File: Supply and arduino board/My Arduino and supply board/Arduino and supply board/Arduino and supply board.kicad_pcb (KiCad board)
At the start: 2 copper layers, 65 parts, among them IC1 MC33269ST-5.0T3, IC2 MC33269D-5.0, J1 Barrel_Jack_MountingPin, Q1 16MHz, Q2 16MHz, T1 FDN340V, U1 LP2985-3.3, U1A1 LM358D, U1B1 LM358D, U1C1 LM358D, U3 ATmega16U2-MU, X1 USB_B, Y1 16MHz, Y2 16MHz

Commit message: new work on arduino board
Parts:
- added @HOLE0: , , F.Cu at (198.3, 64.1)
- added @HOLE1: , , F.Cu at (198.3, 92.1)
- added @HOLE2: , , F.Cu at (147.5, 48.9)
- added @HOLE3: , , F.Cu at (146.2, 97.1)
- moved ZIC1 149.8 mm to (196.1, 79.7), turned to 270 degrees
- moved IOL1 130.4 mm to (195.7, 48.9), turned to 270 degrees
- moved AD1 122.1 mm to (183.0, 97.2), turned to 90 degrees
- moved IOH1 113.4 mm to (174.1, 48.9), turned to 270 degrees
- moved ISCP2 111.7 mm to (195.8, 69.2)
- moved RN2B1 111.6 mm to (162.8, 53.3), turned to 90 degrees
- moved Q2 108.1 mm to (169.1, 57.2)
- moved POWER1 101.7 mm to (165.2, 97.2), turned to 90 degrees
- moved R3 96.9 mm to (151.6, 70.9)
- moved U1 95.7 mm to (175.5, 62.7)
- moved R1 84.6 mm to (153.7, 70.9)
- moved TX_YELLOW1 82.0 mm to (162.5, 67.1)
- moved X1 76.7 mm to (138.6, 61.6), turned to 270 degrees
- moved C5 74.8 mm to (160.6, 60.2), turned to 270 degrees
- moved PC1 74.7 mm to (150.0, 90.8), turned to 90 degrees
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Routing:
- net GND: track 0.00 -> 242.6 mm, vias 0 -> 3
- net +5V: track 0.00 -> 146.2 mm
- net /SCK: track 0.00 -> 128.6 mm, vias 0 -> 1
- net /MISO: track 0.00 -> 123.6 mm
- net /MOSI: track 0.00 -> 115.6 mm
- net /AREF: track 0.00 -> 106.2 mm
- net /RESET: track 0.00 -> 76.2 mm
- net /SS: track 0.00 -> 65.7 mm
- net /XTAL2: track 0.00 -> 61.5 mm, vias 0 -> 1
- net /IO9: track 0.00 -> 59.1 mm
- net /VIN: track 0.00 -> 51.9 mm
- net /IO8: track 0.00 -> 50.8 mm
- net /IO7: track 0.00 -> 45.9 mm
- net /IO6: track 0.00 -> 43.1 mm
- net /IO5: track 0.00 -> 40.2 mm
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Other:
- board outline added: 68.6 x 53.3 mm
- rule pad_to_mask_clearance: 0 -> 0.051
- board text added: "#"
- board text added: "0"
- board text added: "1"
- board text added: "10"
- board text added: "2"
- board text added: "2011-3-02"
- board text added: "3"
- board text added: "3V3"
- board text added: "4"
- board text added: "5"
- board text added: "5V"
- board text added: "6"
- board text added: "7"
- board text added: "8"
- board text added: "9"
- board text added: "A0"
- board text added: "A1"
- board text added: "A2"
- board text added: "A3"
- board text added: "A4"
- board text added: "A5"
- board text added: "ANALOG IN"
- board text added: "AREF"
- board text added: "D.Cuartielles"
- board text added: "D.Mellis"
- board text added: "D:/SmartProjects/Snc/a4_bn_logo2.bmp"
- board text added: "G.Martino"
- board text added: "GND"
- board text added: "IOREF"
- board text added: "ITALY"
- board text added: "M.Banzi"
- board text added: "MADE IN"
- board text added: "RESET"
- board text added: "RX"
- board text added: "SCL"
- board text added: "SDA"
- board text added: "T.Igoe"
- board text added: "TX"
- board text added: "VIN"

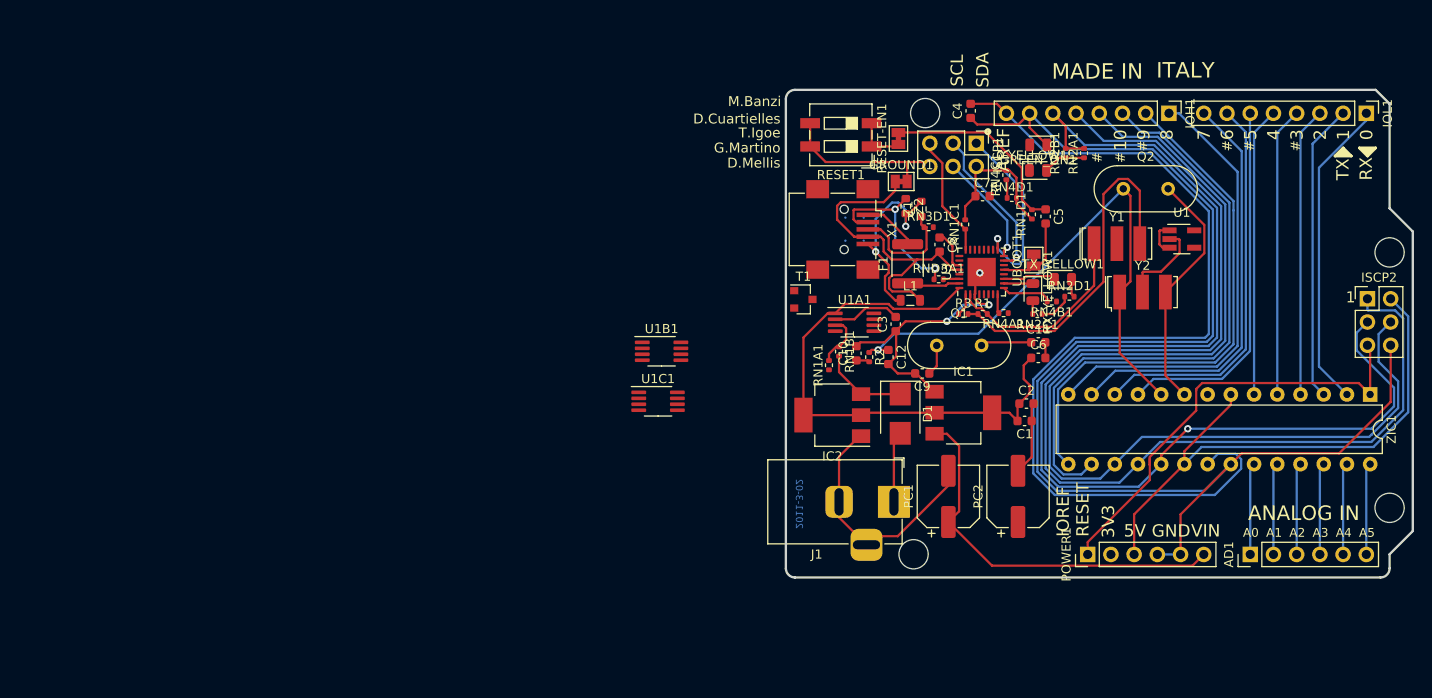
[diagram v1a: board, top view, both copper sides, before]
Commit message: every part on board is connected
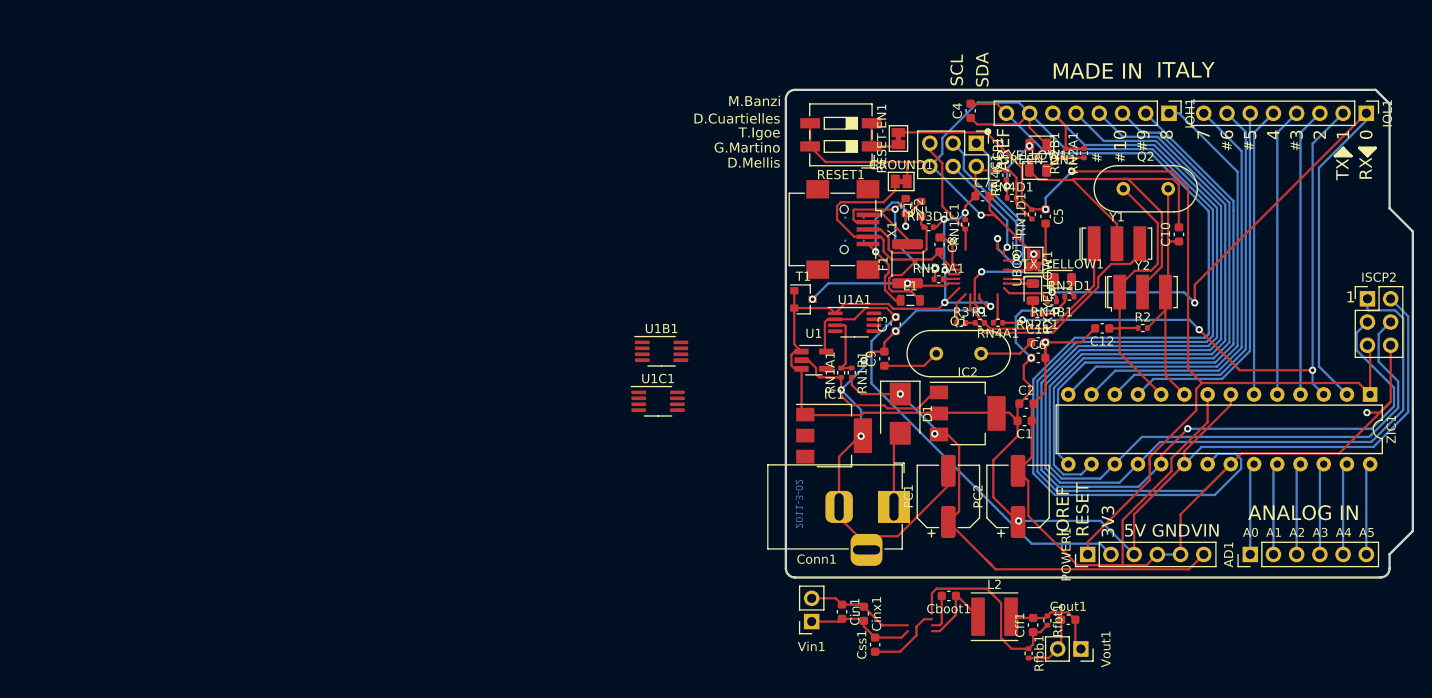
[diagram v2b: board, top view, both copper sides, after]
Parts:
- removed @HOLE0, @HOLE1, @HOLE2, @HOLE3: , 
- removed J1: Barrel_Jack_MountingPin, Connector_BarrelJack:BarrelJack_Horizontal
- removed U3: ATmega16U2-MU, Package_DFN_QFN:QFN-32-1EP_5x5mm_P0.5mm_EP3.1x3.1mm
- added Cboot1: 100n, Capacitor_SMD:C_0603_1608Metric, F.Cu at (150.0, 101.7)
- added Cff1: 47p, Capacitor_SMD:C_0603_1608Metric, F.Cu at (159.3, 104.9)
- added Cin1: 10u, Capacitor_SMD:C_0603_1608Metric, F.Cu at (138.4, 103.4)
- added Cinx1: 100n, Capacitor_SMD:C_0603_1608Metric, F.Cu at (140.7, 103.6)
- added Conn1: Connector_Barrel_Jack_MountingPin-Arduino_and_supply_board-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, Connector_BarrelJack:BarrelJack_Horizontal, F.Cu at (144.0, 92.0)
- added Cout1: 47u, Capacitor_SMD:C_0603_1608Metric, F.Cu at (163.1, 104.3)
- added Css1: 33n, Capacitor_SMD:C_0603_1608Metric, F.Cu at (142.0, 107.0)
- added L2: 15u, Inductor_SMD:L_Taiyo-Yuden_MD-5050, F.Cu at (155.0, 104.0)
- added Rfbb1: 10K, Resistor_SMD:R_0402_1005Metric, F.Cu at (158.8, 108.0)
- added Rfbt1: 140K, Resistor_SMD:R_0402_1005Metric, F.Cu at (160.8, 104.4)
- added Vin1: Conn_01x02, Connector_PinSocket_2.54mm:PinSocket_1x02_P2.54mm_Vertical, F.Cu at (135.0, 104.5)
- added Vout1: Conn_01x02, Connector_PinSocket_2.54mm:PinSocket_1x02_P2.54mm_Vertical, F.Cu at (164.5, 107.5)
- IC1: value MC33269ST-5.0T3 -> MC33269ST-5.0T3-Arduino_and_supply_board-cache
- IC2: value MC33269D-5.0 -> MC33269D-5.0-Arduino_and_supply_board-cache
- moved U1 42.4 mm to (135.3, 75.9)
- moved C10 37.6 mm to (175.2, 62.1)
- moved R2 30.1 mm to (171.3, 72.4), turned to 0 degrees
- moved C12 23.6 mm to (166.8, 72.4), turned to 180 degrees
- moved IC2 14.8 mm to (152.1, 81.7), turned to 0 degrees
- moved IC1 14.4 mm to (137.5, 84.2)
- moved C9 4.44 mm to (143.0, 75.7), turned to 90 degrees
- moved RN1B1 2.70 mm to (139.4, 77.3)
- moved RN1A1 1.56 mm to (138.3, 77.3)
- moved RN4A1 1.22 mm to (155.4, 71.8)
- moved R1 1.02 mm to (153.4, 71.8)
- moved R3 0.99 mm to (151.4, 71.8)
- moved Q1 0.89 mm to (148.7, 75.2)
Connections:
- C8 pad 1: /VUCAP -> (no net)
- ISCP1 pad 1: /MISO2 -> (no net)
- ISCP1 pad 3: /SCK2 -> (no net)
- ISCP1 pad 4: /MOSI2 -> (no net)
- R3 pad 1: Net-(R3-Pad1) -> (no net)
- RN4A1 pad 2: /M8TXD -> (no net)
- RN4B1 pad 2: /M8RXD -> (no net)
- RND3A1 pad 2: /RD- -> (no net)
- RX_YELLOW1 pad 1: /RXLED -> (no net)
- TX_YELLOW1 pad 1: /TXLED -> (no net)
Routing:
- net GND: track 242.6 -> 421.3 mm, vias 3 -> 10
- net +5V: track 146.2 -> 209.5 mm, vias 0 -> 8
- net /+3V3: track 7.52 -> 54.4 mm, vias 0 -> 1
- net /IO0: track 34.2 -> 80.0 mm, vias 0 -> 2
- net /RESET: track 76.2 -> 117.0 mm, vias 0 -> 2
- net /IO1: track 32.6 -> 69.1 mm, vias 0 -> 3
- net /XTAL2: track 61.5 -> 32.0 mm, vias 1 -> 0
- net Net-(Cff1-Pad1): track 0.00 -> 21.9 mm
- net Net-(R1-Pad1): track 38.4 -> 25.6 mm
- net Net-(Cin1-Pad1): track 0.00 -> 11.8 mm
- net Net-(Cff1-Pad2): track 0.00 -> 11.1 mm
- net /USBVCC: track 5.87 -> 17.0 mm, vias 0 -> 2
- net Net-(Cboot1-Pad1): track 0.00 -> 8.80 mm
- net Net-(Css1-Pad1): track 0.00 -> 8.23 mm
- net Net-(GREEN_ON1-Pad2): track 2.03 -> 7.43 mm, vias 0 -> 2
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
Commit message: new work on board
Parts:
- added U4: Arduino_and_supply_board-cache_Arduino_and_supply_board-cac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, Package_TO_SOT_SMD:TSOT-23-8, F.Cu at (142.6, 100.9)
- moved Cout1 22.0 mm to (141.4, 107.3)
- moved Rfbb1 17.7 mm to (144.1, 98.0), turned to 90 degrees
- moved Rfbt1 16.7 mm to (145.3, 98.1)
- moved Cff1 14.4 mm to (146.8, 97.6)
- moved Vout1 13.7 mm to (150.8, 107.0), turned to 180 degrees
- moved L2 9.41 mm to (145.8, 105.9), turned to 270 degrees
- moved Css1 8.65 mm to (147.0, 100.0), turned to 0 degrees
- moved Cboot1 3.08 mm to (147.0, 101.7)
- moved Cinx1 1.75 mm to (139.5, 102.4)
- moved Cin1 1.17 mm to (137.8, 102.4)
- moved Vin1 0.73 mm to (135.0, 105.2)
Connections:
- Cboot1 pad 2: (no net) -> Net-(Cboot1-Pad2)
- Css1 pad 1: (no net) -> Net-(Css1-Pad1)
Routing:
- net (no net): track 0.09 -> 77.8 mm, vias 0 -> 3
- net /MISO2: track 20.9 -> 0.00 mm, vias 1 -> 0
- net Net-(Cff1-Pad1): track 21.9 -> 4.30 mm
- net GND: track 421.3 -> 438.3 mm
- net /SCK2: track 16.9 -> 0.00 mm, vias 1 -> 0
- net /MOSI2: track 12.4 -> 0.00 mm, vias 1 -> 0
- net Net-(Cff1-Pad2): track 11.1 -> 22.3 mm, vias 0 -> 2
- net /TXLED: track 5.79 -> 0.00 mm
- net Net-(Css1-Pad1): track 8.23 -> 2.59 mm
- net /M8RXD: track 5.53 -> 0.00 mm
- net Net-(Cin1-Pad1): track 11.8 -> 6.88 mm
- net /VUCAP: track 4.48 -> 0.00 mm
- net Net-(R3-Pad1): track 3.54 -> 0.00 mm
- net /M8TXD: track 3.32 -> 0.00 mm
- net /RXLED: track 3.17 -> 0.00 mm
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- added copper zone on F.Cu, net Net-(Cboot1-Pad1)
- added copper zone on F.Cu, net Net-(Cboot1-Pad2)
- added copper zone on F.Cu, net Net-(Cff1-Pad1)
- added copper zone on F.Cu, net Net-(Cff1-Pad2)
- added copper zone on F.Cu, net Net-(Cin1-Pad1)
- added copper zone on F.Cu, net Net-(Css1-Pad1)
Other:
- board size 68.6 x 53.3 mm -> 68.6 x 63.5 mm

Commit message: big changes on arduino board
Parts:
- removed AD1: Conn_01x06, Connector_PinHeader_2.54mm:PinHeader_1x06_P2.54mm_Vertical
- removed C11: 22p, Capacitor_SMD:C_0603_1608Metric
- removed Conn1: Connector_Barrel_Jack_MountingPin-Arduino_and_supply_board-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, Connector_BarrelJack:BarrelJack_Horizontal
- removed F1: 500mA, Resistor_SMD:R_1812_4532Metric
- removed GROUND1, RESET-EN1, UBOOT1: SolderJumper_2_Bridged, Jumper:SolderJumper-2_P1.3mm_Bridged_Pad1.0x1.5mm
- removed IC1: MC33269ST-5.0T3-Arduino_and_supply_board-cache, Package_TO_SOT_SMD:SOT-223
- removed IC2: MC33269D-5.0-Arduino_and_supply_board-cache, Package_TO_SOT_SMD:SOT-223-3_TabPin2
- removed IOH1, IOL1: Conn_01x08, Connector_PinHeader_2.54mm:PinHeader_1x08_P2.54mm_Vertical
- removed ISCP1, ISCP2: ISCP, Connector_PinHeader_2.54mm:PinHeader_2x03_P2.54mm_Vertical
- removed L1: BLM21, Inductor_SMD:L_0805_2012Metric
- removed Q1: 16MHz, Crystal:Crystal_HC18-U_Vertical
- removed RN1C1: 10K, Resistor_SMD:R_0402_1005Metric
- removed RN2A1, RN2B1, RN4C1: 1K, Resistor_SMD:R_0402_1005Metric
- removed RN3D1, RND3A1: 22R, Resistor_SMD:R_0402_1005Metric
- removed U1A1, U1B1, U1C1: LM358D, Package_SO:MSOP-8_3x3mm_P0.65mm
- removed X1: USB_B, Connector_USB:USB_Mini-B_Wuerth_65100516121_Horizontal
- removed Y1: 16MHz, Crystal:Resonator_SMD-3Pin_7.2x3.0mm
- removed YELLOW1: LED, LED_SMD:LED_0805_2012Metric
- removed Z1, Z2: PGB1010604, Resistor_SMD:R_0603_1608Metric
- removed ZIC1: ATmega328P-PU, Package_DIP:DIP-28_W7.62mm
- added FB1: Ferrite_Bead, Resistor_SMD:R_0603_1608Metric, F.Cu at (143.2, 57.0)
- added J1: USB_C_Receptacle_USB2.0, Connector_USB:USB_C_Receptacle_HRO_TYPE-C-31-M-12, F.Cu at (136.3, 61.3)
- added J2: Conn_01x03, Connector_PinSocket_2.54mm:PinSocket_1x03_P2.54mm_Vertical, F.Cu at (169.2, 60.5)
- added J3: Conn_01x03, Connector_PinSocket_2.54mm:PinSocket_1x03_P2.54mm_Vertical, F.Cu at (169.2, 64.2)
- added J4: Conn_01x03, Connector_PinSocket_2.54mm:PinSocket_1x03_P2.54mm_Vertical, F.Cu at (169.2, 68.0)
- added J5: Conn_01x03, Connector_PinSocket_2.54mm:PinSocket_1x03_P2.54mm_Vertical, F.Cu at (169.2, 71.7)
- added J6: Conn_01x03, Connector_PinSocket_2.54mm:PinSocket_1x03_P2.54mm_Vertical, F.Cu at (169.2, 75.5)
- added J7: Conn_01x03, Connector_PinSocket_2.54mm:PinSocket_1x03_P2.54mm_Vertical, F.Cu at (169.2, 79.2)
- added U2: LP2985-3.3, Package_TO_SOT_SMD:SOT-23-5_HandSoldering, F.Cu at (151.4, 72.5)
- added U3: MC33269D-5.0, Package_TO_SOT_SMD:SOT-223-3_TabPin2, F.Cu at (161.4, 79.2)
- added U5: TPS629DRL, Package_TO_SOT_SMD:TSOT-23-8, F.Cu at (142.4, 94.2)
- added U7: Atmega328P-PU, Package_QFP:TQFP-32_7x7mm_P0.8mm, F.Cu at (160.4, 62.0)
- added U8: FT231XQ, Package_DFN_QFN:QFN-20-1EP_4x4mm_P0.5mm_EP2.5x2.5mm, F.Cu at (148.7, 60.9)
- added Vin2: Conn_01x02, Connector_PinSocket_2.54mm:PinSocket_1x02_P2.54mm_Vertical, F.Cu at (134.7, 74.5)
- C5: value 100n -> 10n
- C7: value 100n -> 47p
- C8: value 1u -> 47p
- C9: value 22p -> 100n
- R1: value 1M -> 27R
- U1: value LP2985-3.3 -> LM358D; footprint Package_TO_SOT_SMD:SOT-23-5_HandSoldering -> Package_SO:MSOP-8_3x3mm_P0.65mm
- U4: value Arduino_and_supply_board-cache_Arduino_and_supply_board-cache_TPS629DRL -> MC33269ST-5.0T3; footprint Package_TO_SOT_SMD:TSOT-23-8 -> Package_TO_SOT_SMD:SOT-223
- moved POWER1 52.8 mm to (144.9, 48.4)
- moved U4 24.4 mm to (153.7, 79.2), turned to 270 degrees
- moved C4 22.9 mm to (161.9, 69.5), turned to 180 degrees
- moved R2 22.7 mm to (164.7, 50.7)
- moved C1 22.4 mm to (137.4, 74.5), turned to 270 degrees
- moved C12 21.7 mm to (158.9, 52.2)
- moved C5 19.1 mm to (142.4, 66.0)
- moved Y2 16.5 mm to (164.4, 53.5)
- moved T1 15.6 mm to (147.9, 76.5)
- moved GREEN_ON1 15.3 mm to (144.7, 54.7), turned to 0 degrees
- moved R1 14.9 mm to (144.2, 60.2), turned to 180 degrees
- moved R9 14.3 mm to (148.9, 69.2), turned to 90 degrees
- moved R13 13.1 mm to (152.7, 59.0)
- moved TX_YELLOW1 13.1 mm to (149.4, 66.2), turned to 270 degrees
- moved RX_YELLOW1 12.3 mm to (147.2, 66.2)
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- renumbered Cin1 to C13, Cinx1 to C14, Css1 to C15, Cboot1 to C16, Cff1 to C17, Cout1 to C18, RN2C1 to R10, RN1D1 to R11, RN4B1 to R12, RN4A1 to R13, RN4D1 to R16, Rfbt1 to R18, Rfbb1 to R19, RN1B1 to R4, RN1A1 to R5, RN2D1 to R9
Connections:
- C13 pad 1: Net-(Cin1-Pad1) -> Net-(C13-Pad1)
- C14 pad 1: Net-(Cin1-Pad1) -> Net-(C13-Pad1)
- C15 pad 1: Net-(Css1-Pad1) -> Net-(C15-Pad1)
- C16 pad 1: Net-(Cboot1-Pad1) -> Net-(C16-Pad1)
- C16 pad 2: Net-(Cboot1-Pad2) -> Net-(C16-Pad2)
- C17 pad 1: Net-(Cff1-Pad1) -> Net-(C17-Pad1)
- C5 pad 1: /RESET -> Net-(C5-Pad1)
- C5 pad 2: /DTR -> GND
- C7 pad 1: +5V -> Net-(C7-Pad1)
- C8 pad 1: (no net) -> Net-(C8-Pad1)
- C8 pad 2: /UGND -> GND
- C9 pad 1: /XT1 -> Net-(C9-Pad1)
- L2 pad 1: Net-(Cboot1-Pad1) -> Net-(C16-Pad1)
- R1 pad 2: Net-(R1-Pad2) -> Net-(C7-Pad1)
- R12 pad 1: /IO0 -> Net-(R12-Pad1)
- R12 pad 2: (no net) -> /M8RXD
- R13 pad 1: /IO1 -> Net-(R13-Pad1)
- R13 pad 2: (no net) -> /M8TXD
- R18 pad 2: Net-(Cff1-Pad1) -> Net-(C17-Pad1)
- R19 pad 1: Net-(Cff1-Pad1) -> Net-(C17-Pad1)
- R3 pad 1: (no net) -> Net-(R3-Pad1)
- R3 pad 2: Net-(R1-Pad1) -> Net-(C8-Pad1)
- RX_YELLOW1 pad 1: (no net) -> /RXLED
- TX_YELLOW1 pad 1: (no net) -> /TXLED
- U1 pad 2: GND -> /+3V3
- U1 pad 3: +5V -> /CMP
- U1 pad 4: (no net) -> GND
- U1 pad 5: /+3V3 -> GND
- U4 pad 1: (no net) -> GND
- U4 pad 2: (no net) -> +5V
- U4 pad 3: Net-(Cin1-Pad1) -> /VIN
- U4 pad 4: GND -> +5V
- Vin1 pad 2: Net-(Cin1-Pad1) -> Net-(C13-Pad1)
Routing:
- net GND: track 438.3 -> 88.5 mm, vias 10 -> 0
- net +5V: track 209.5 -> 71.9 mm, vias 8 -> 0
- net /SCK: track 128.6 -> 0.00 mm, vias 1 -> 0
- net /MISO: track 123.6 -> 0.00 mm
- net /MOSI: track 115.6 -> 0.00 mm
- net /RESET: track 117.0 -> 10.5 mm, vias 2 -> 0
- net /AREF: track 106.2 -> 3.38 mm
- net /IO0: track 80.0 -> 0.00 mm, vias 2 -> 0
- net (no net): track 77.8 -> 0.00 mm, vias 3 -> 0
- net /IO1: track 69.1 -> 0.00 mm, vias 3 -> 0
- net /SS: track 65.7 -> 0.00 mm
- net /IO9: track 59.1 -> 0.00 mm
- net /IO8: track 50.8 -> 0.00 mm
- net /IO7: track 45.9 -> 0.00 mm
- net /IO6: track 43.1 -> 0.00 mm
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- added copper zone on F.Cu, net Net-(C13-Pad1)
- added copper zone on F.Cu, net Net-(C15-Pad1)
- added copper zone on F.Cu, net Net-(C16-Pad1)
- added copper zone on F.Cu, net Net-(C16-Pad2)
- added copper zone on F.Cu, net Net-(C17-Pad1)
- removed copper zone on F.Cu, net Net-(Cboot1-Pad1)
- removed copper zone on F.Cu, net Net-(Cboot1-Pad2)
- removed copper zone on F.Cu, net Net-(Cff1-Pad1)
- removed copper zone on F.Cu, net Net-(Cin1-Pad1)
- removed copper zone on F.Cu, net Net-(Css1-Pad1)
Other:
- outline, holes or cut-outs redrawn
- net class Default: clearance 0.2 -> 0.15
- rule trace_clearance: 0.2 -> 0.15
- board text removed: "2011-3-02"

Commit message: work on arduino board
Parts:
- moved Vout1 17.3 mm to (133.9, 95.5)
- moved Vin1 9.56 mm to (133.9, 89.0)
- moved C18 8.57 mm to (140.9, 92.0)
- moved T1 8.31 mm to (140.2, 73.5)
- moved R5 8.25 mm to (139.9, 68.5)
- moved R4 8.25 mm to (141.2, 68.5)
- moved U1 7.50 mm to (136.2, 69.7)
- moved U2 7.35 mm to (144.4, 70.2)
- moved U4 7.35 mm to (155.9, 72.2)
- moved C3 7.07 mm to (147.9, 72.0), turned to 90 degrees
- moved PC2 7.04 mm to (153.9, 80.7)
- moved C14 6.54 mm to (138.4, 89.2)
- moved C13 6.52 mm to (136.7, 89.2)
- moved POWER1 6.35 mm to (144.9, 42.1)
- moved PC1 6.01 mm to (144.2, 79.2), turned to 90 degrees
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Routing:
- net GND: track 88.5 -> 266.8 mm, vias 0 -> 73
- net +5V: track 71.9 -> 211.1 mm, vias 0 -> 5
- net /VIN: track 36.1 -> 84.7 mm, vias 2 -> 4
- net /RESET: track 10.5 -> 52.0 mm, vias 0 -> 1
- net /+3V3: track 14.7 -> 41.9 mm, vias 0 -> 2
- net Net-(C5-Pad1): track 6.38 -> 13.4 mm
- net Net-(C17-Pad2): track 22.3 -> 26.6 mm, vias 2 -> 0
- net /USBVCC: track 23.5 -> 26.5 mm, vias 3 -> 5
- net /XTAL1: track 27.6 -> 25.2 mm
- net Net-(GREEN_ON1-Pad2): track 0.00 -> 1.62 mm
- net /XTAL2: track 27.2 -> 26.0 mm
- net Net-(C13-Pad1): track 6.88 -> 8.03 mm
- net Net-(R13-Pad1): track 13.3 -> 14.2 mm
- net Net-(C16-Pad1): track 6.49 -> 5.63 mm
- net /CMP: track 3.71 -> 3.06 mm
- added copper zone on F.Cu, net +5V
- added copper zone on F.Cu, net /PWRIM
- added copper zone on B.Cu, net /VIN
- added copper zone on F.Cu, net /VIN
- added copper zone on B.Cu, net GND
- added copper zone on F.Cu, net GND
- removed copper zone on F.Cu, net Net-(C15-Pad1)
- removed copper zone on F.Cu, net Net-(C16-Pad2)
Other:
- board size 68.6 x 63.5 mm -> 44.5 x 57.2 mm
